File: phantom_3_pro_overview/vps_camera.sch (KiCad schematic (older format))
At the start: 0 parts

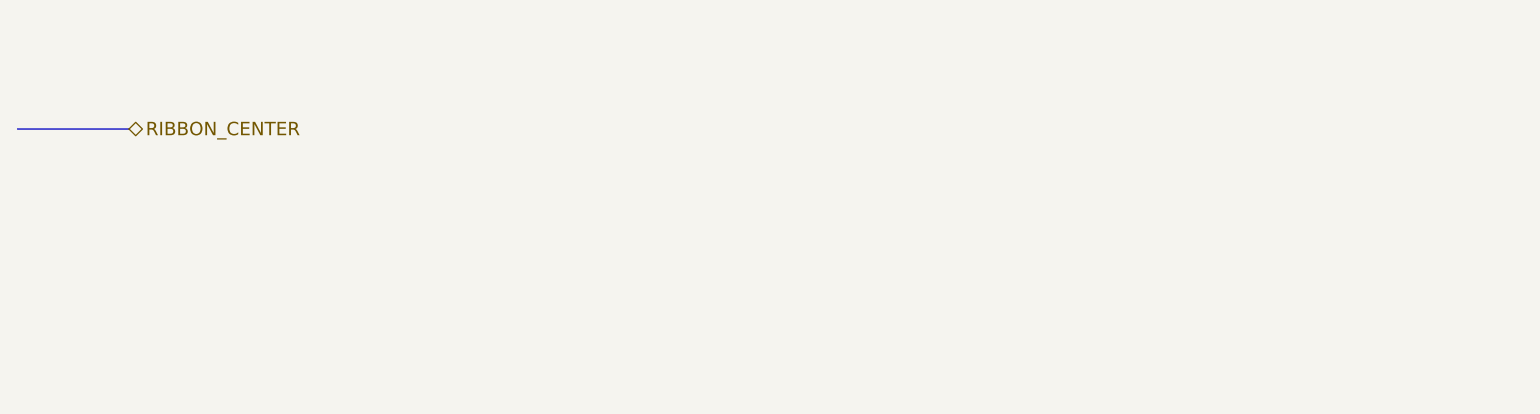
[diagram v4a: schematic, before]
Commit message: Overview: Updated VPS definition.
Placed proper components into VPS schematics.
No connections are made between components yet.
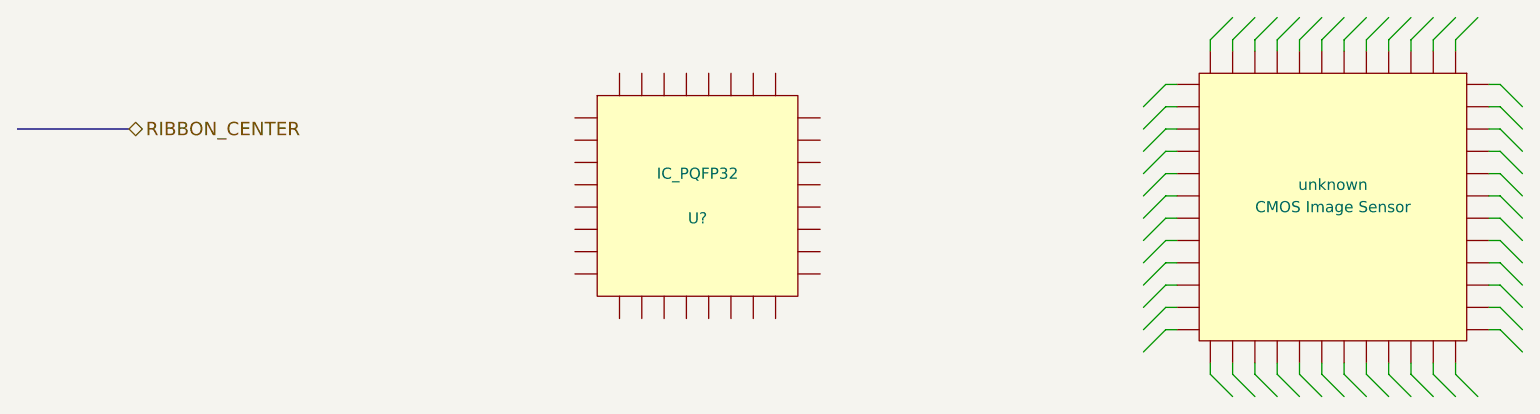
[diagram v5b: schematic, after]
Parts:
- added U?: unknown, CMOS Image Sensor, symbol IC_PQFP48
- added U?: IC_PQFP32, MODULE, symbol IC_PQFP32
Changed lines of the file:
@@
 $Descr A4 11693 8268
 encoding utf-8
-Sheet 20 23
+Sheet 8 23
 Title "Overview of the Phantom 3 Pro VPS Camera"
 Date ""
@@
 Text HLabel 3050 1850 2    60   BiDi ~ 0
 RIBBON_CENTER
+$Comp
+L IC_PQFP48 U?
+U 1 1 597EFE0C
+P 8450 2200
+F 0 "U?" H 8450 2100 50  0001 C CNN
+F 1 "unknown" H 8450 2300 50  0000 C CNN
+F 2 "CMOS Image Sensor" H 8450 2200 50  0000 C CNN
+F 3 "DOCUMENTATION" H 8450 2200 50  0001 C CNN
+	1    8450 2200
+	1    0    0    -1
+$EndComp
+Entry Wire Line
+	9200 1650 9300 1750
+Entry Wire Line
+	9200 1750 9300 1850
+Entry Wire Line
+	9200 1850 9300 1950
+Entry Wire Line
+	9200 1950 9300 2050
+Entry Wire Line
+	9200 2050 9300 2150
+Entry Wire Line
+	9200 2150 9300 2250
+Entry Wire Line
+	9200 2250 9300 2350
+Entry Wire Line
+	9200 2350 9300 2450
+Entry Wire Line
+	9200 2450 9300 2550
+Entry Wire Line
+	9200 2550 9300 2650
+Entry Wire Line
+	9200 2650 9300 2750
+Entry Wire Line
+	9200 2750 9300 2850
+Wire Wire Line
+	9150 1650 9200 1650
+Wire Wire Line
+	9200 1750 9150 1750
+Wire Wire Line
+	9150 1850 9200 1850
+Wire Wire Line
+	9200 1950 9150 1950
+Wire Wire Line
+	9150 2050 9200 2050
+Wire Wire Line
+	9150 2150 9200 2150
+Wire Wire Line
+	9200 2250 9150 2250
+Wire Wire Line
+	9150 2350 9200 2350
+Wire Wire Line
+	9200 2450 9150 2450
+Wire Wire Line
+	9150 2550 9200 2550
+Wire Wire Line
+	9200 2650 9150 2650
+Wire Wire Line
+	9150 2750 9200 2750
+Entry Wire Line
+	7900 1450 8000 1350
+Entry Wire Line
+	8000 1450 8100 1350
+Entry Wire Line
+	8100 1450 8200 1350
+Entry Wire Line
+	8200 1450 8300 1350
+Entry Wire Line
+	8300 1450 8400 1350
+Entry Wire Line
+	8400 1450 8500 1350
+Entry Wire Line
+	8500 1450 8600 1350
+Entry Wire Line
+	8600 1450 8700 1350
+Entry Wire Line
+	8700 1450 8800 1350
+Entry Wire Line
+	8800 1450 8900 1350
+Entry Wire Line
+	8900 1450 9000 1350
+Entry Wire Line
+	9000 1450 9100 1350
+Wire Wire Line
+	7900 1500 7900 1450
+Wire Wire Line
+	8000 1450 8000 1500
+Wire Wire Line
+	8100 1500 8100 1450
+Wire Wire Line
+	8200 1450 8200 1500
+Wire Wire Line
+	8300 1500 8300 1450
+Wire Wire Line
+	8400 1500 8400 1450
+Wire Wire Line
+	8500 1450 8500 1500
+Wire Wire Line
+	8600 1500 8600 1450
+Wire Wire Line
+	8700 1450 8700 1500
+Wire Wire Line
+	8800 1500 8800 1450
+Wire Wire Line
+	8900 1450 8900 1500
+Wire Wire Line
+	9000 1500 9000 1450
+Entry Wire Line
+	7700 1650 7600 1750
+Entry Wire Line
+	7700 1750 7600 1850
+Entry Wire Line
+	7700 1850 7600 1950
+Entry Wire Line
+	7700 1950 7600 2050
+Entry Wire Line
+	7700 2050 7600 2150
+Entry Wire Line
+	7700 2150 7600 2250
+Entry Wire Line
+	7700 2250 7600 2350
+Entry Wire Line
+	7700 2350 7600 2450
+Entry Wire Line
+	7700 2450 7600 2550
+Entry Wire Line
+	7700 2550 7600 2650
+Entry Wire Line
+	7700 2650 7600 2750
+Entry Wire Line
+	7700 2750 7600 2850
+Wire Wire Line
+	7750 1650 7700 1650
+Wire Wire Line
+	7700 1750 7750 1750
+Wire Wire Line
+	7750 1850 7700 1850
+Wire Wire Line
+	7700 1950 7750 1950
+Wire Wire Line
+	7750 2050 7700 2050
+Wire Wire Line
+	7750 2150 7700 2150
+Wire Wire Line
+	7700 2250 7750 2250
+Wire Wire Line
+	7750 2350 7700 2350
+Wire Wire Line
+	7700 2450 7750 2450
+Wire Wire Line
+	7750 2550 7700 2550
+Wire Wire Line
+	7700 2650 7750 2650
+Wire Wire Line
+	7750 2750 7700 2750
+Entry Wire Line
+	7900 2950 8000 3050
+Entry Wire Line
+	8000 2950 8100 3050
+Entry Wire Line
+	8100 2950 8200 3050
+Entry Wire Line
+	8200 2950 8300 3050
+Entry Wire Line
+	8300 2950 8400 3050
+Entry Wire Line
+	8400 2950 8500 3050
+Entry Wire Line
+	8500 2950 8600 3050
+Entry Wire Line
+	8600 2950 8700 3050
+Entry Wire Line
+	8700 2950 8800 3050
+Entry Wire Line
+	8800 2950 8900 3050
+Entry Wire Line
+	8900 2950 9000 3050
+Entry Wire Line
+	9000 2950 9100 3050
+Wire Wire Line
+	7900 2900 7900 2950
+Wire Wire Line
+	8000 2950 8000 2900
+Wire Wire Line
+	8100 2900 8100 2950
+Wire Wire Line
+	8200 2950 8200 2900
+Wire Wire Line
+	8300 2900 8300 2950
+Wire Wire Line
+	8400 2900 8400 2950
+Wire Wire Line
+	8500 2950 8500 2900
+Wire Wire Line
+	8600 2900 8600 2950
+Wire Wire Line
+	8700 2950 8700 2900
+Wire Wire Line
+	8800 2900 8800 2950
+Wire Wire Line
+	8900 2950 8900 2900
+Wire Wire Line
+	9000 2900 9000 2950
+$Comp
+L IC_PQFP32 U?
+U 1 1 597F013F
+P 5600 2150
+F 0 "U?" H 5600 2050 50  0000 C CNN
+F 1 "IC_PQFP32" H 5600 2250 50  0000 C CNN
+F 2 "MODULE" H 5600 2150 50  0001 C CNN
+F 3 "DOCUMENTATION" H 5600 2150 50  0001 C CNN
+	1    5600 2150
+	1    0    0    -1
+$EndComp
 $EndSCHEMATC

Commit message: Overview: Upgraded to KiCAD 5.0.1.
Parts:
- U?: symbol IC_PQFP48 -> ic_dil_generic:IC_PQFP48
- U?: symbol IC_PQFP32 -> ic_dil_generic:IC_PQFP32
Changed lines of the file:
@@
-EESchema Schematic File Version 2
-LIBS:power
-LIBS:device
-LIBS:transistors
-LIBS:conn
-LIBS:linear
-LIBS:regul
-LIBS:74xx
-LIBS:cmos4000
-LIBS:adc-dac
-LIBS:memory
-LIBS:xilinx
-LIBS:microcontrollers
-LIBS:dsp
-LIBS:microchip
-LIBS:analog_switches
-LIBS:motorola
-LIBS:texas
-LIBS:intel
-LIBS:audio
-LIBS:interface
-LIBS:digital-audio
-LIBS:philips
-LIBS:display
-LIBS:cypress
-LIBS:siliconi
-LIBS:opto
-LIBS:atmel
-LIBS:contrib
-LIBS:valves
-LIBS:motors
-LIBS:ic_dil_generic
-LIBS:sensors
-LIBS:u-blox
-LIBS:amplifiers
-LIBS:transistors-switches
-LIBS:transistors-power
-LIBS:sensors-v2
-LIBS:regul-v2
+EESchema Schematic File Version 4
 LIBS:phantom_3_pro_overview-cache
-EELAYER 25 0
+EELAYER 26 0
 EELAYER END
 $Descr A4 11693 8268
@@
 RIBBON_CENTER
 $Comp
-L IC_PQFP48 U?
+L ic_dil_generic:IC_PQFP48 U?
 U 1 1 597EFE0C
 P 8450 2200
@@
 	9000 2900 9000 2950
 $Comp
-L IC_PQFP32 U?
+L ic_dil_generic:IC_PQFP32 U?
 U 1 1 597F013F
 P 5600 2150
